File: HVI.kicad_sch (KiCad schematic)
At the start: 36 parts, among them J1 Conn_01x02, J2 Conn_01x02, J3 Conn_01x02, U1 VIPER06-SSOP-10

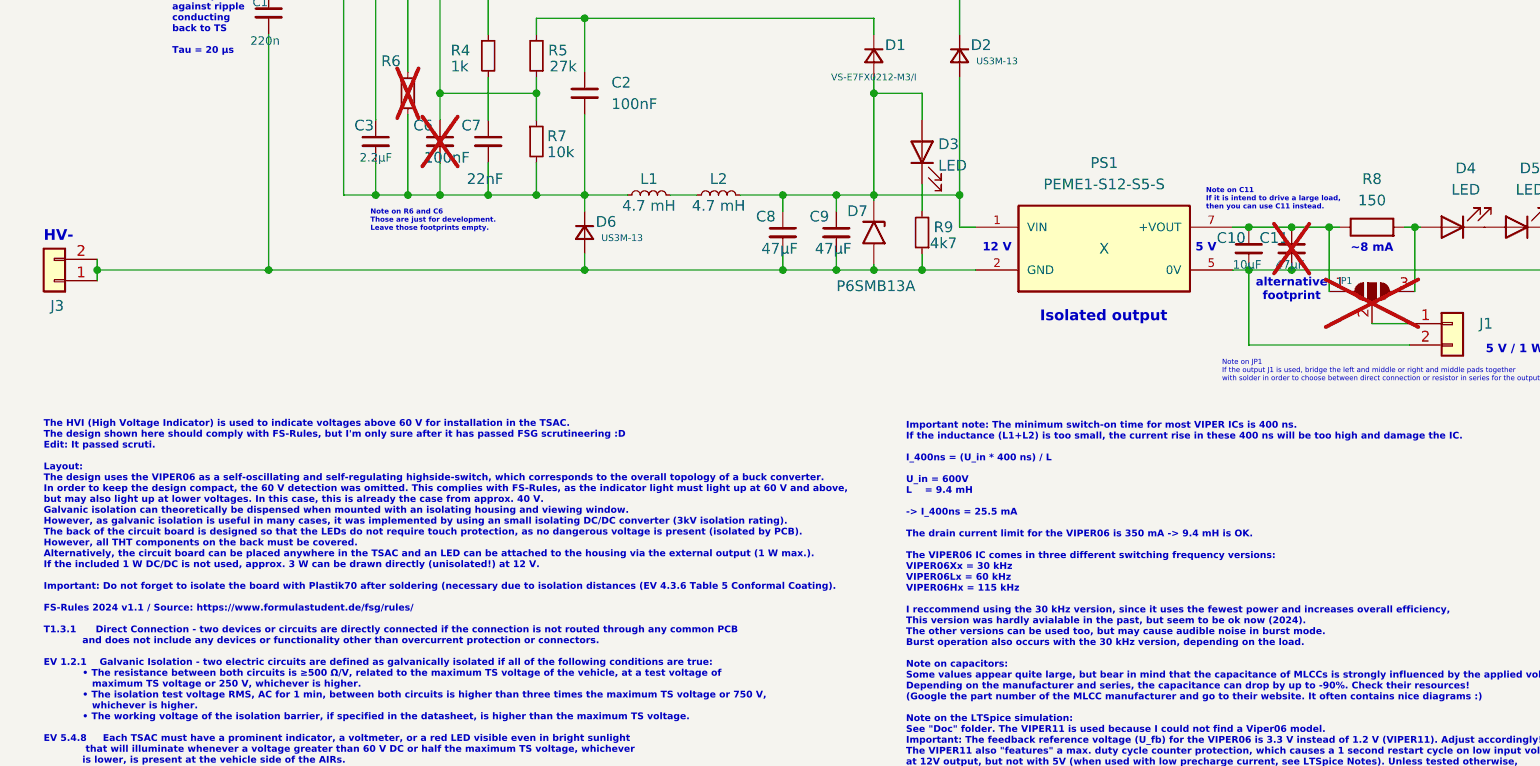
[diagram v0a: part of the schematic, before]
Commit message: Updated PS1 see issue #6
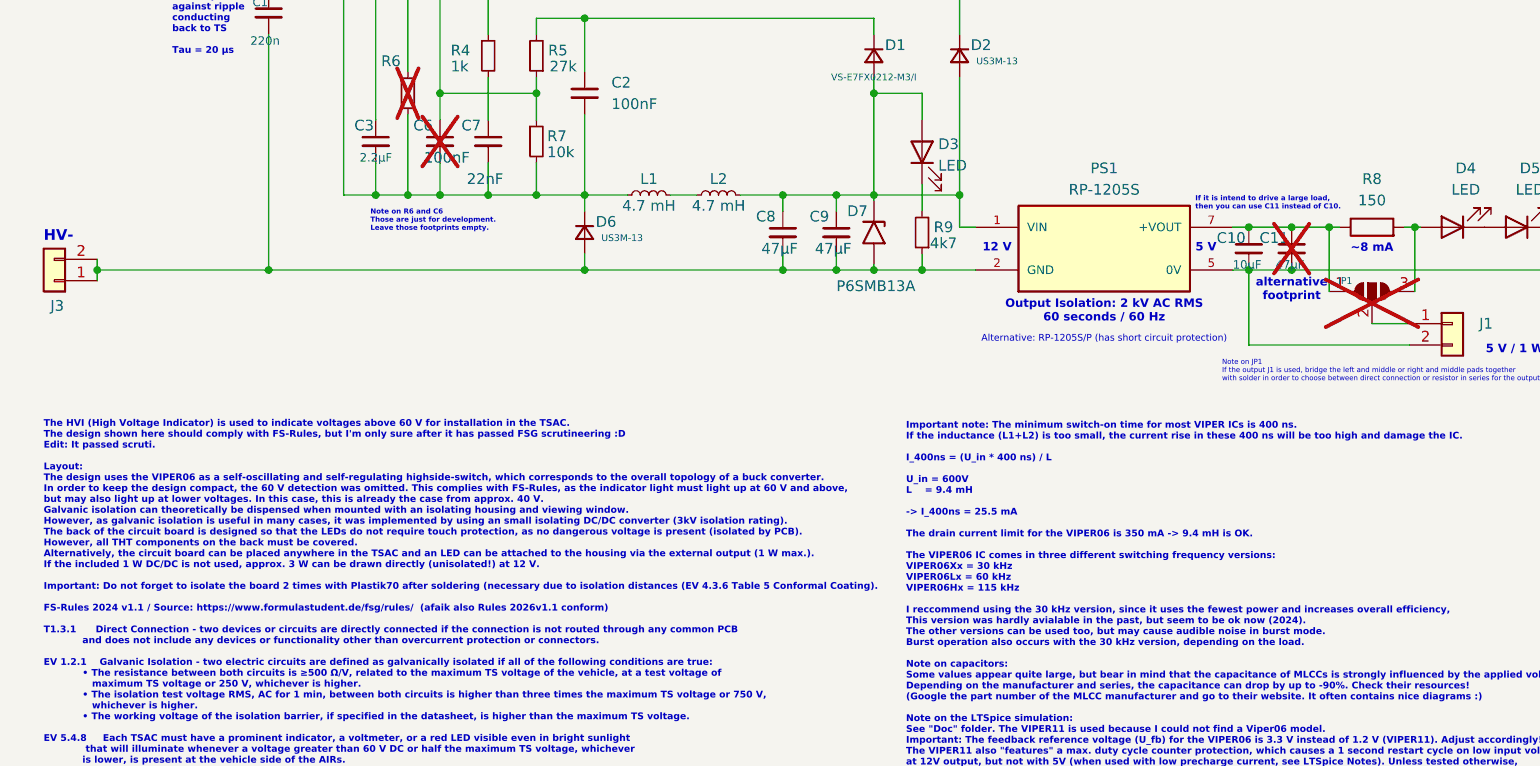
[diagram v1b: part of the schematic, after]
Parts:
- PS1: value PEME1-S12-S5-S -> RP-1205S; MANUFACTURER CUI Inc. -> (none); MAXIMUM_PACKAGE_HEIGHT 10.16mm -> (none); Manufacturer Number PEME1-S12-S5-S -> (none); Mouser 490-PEME1-S12-S5-S -> (none); PARTREV 1.02 -> (none); STANDARD Manufacturer Recommendations -> (none)
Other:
- note added: "Alternative: RP-1205S/P (has short circuit protection)"
- note added: "If it is intend to drive a large load, then you can use C11 instead of C10."
- note added: "Output Isolation: 2 kV AC RMS 60 seconds / 60 Hz"
- note removed: "Isolated output"
- note removed: "Note on C11 If it is intend to drive a large load, then you can use C11 instead."
